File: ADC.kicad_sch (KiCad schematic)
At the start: 14 parts, among them J301 Conn_01x04_Pin, U301 ADS122C04IPW

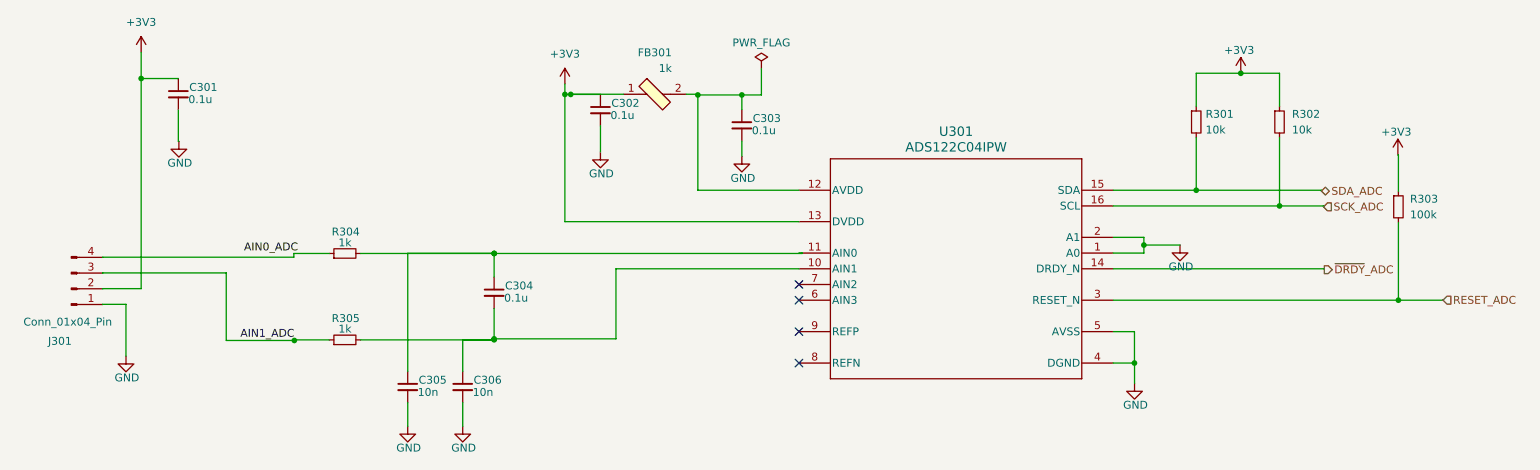
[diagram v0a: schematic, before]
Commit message: critical nets coloured,some tracks rerouted, section 9 completed.
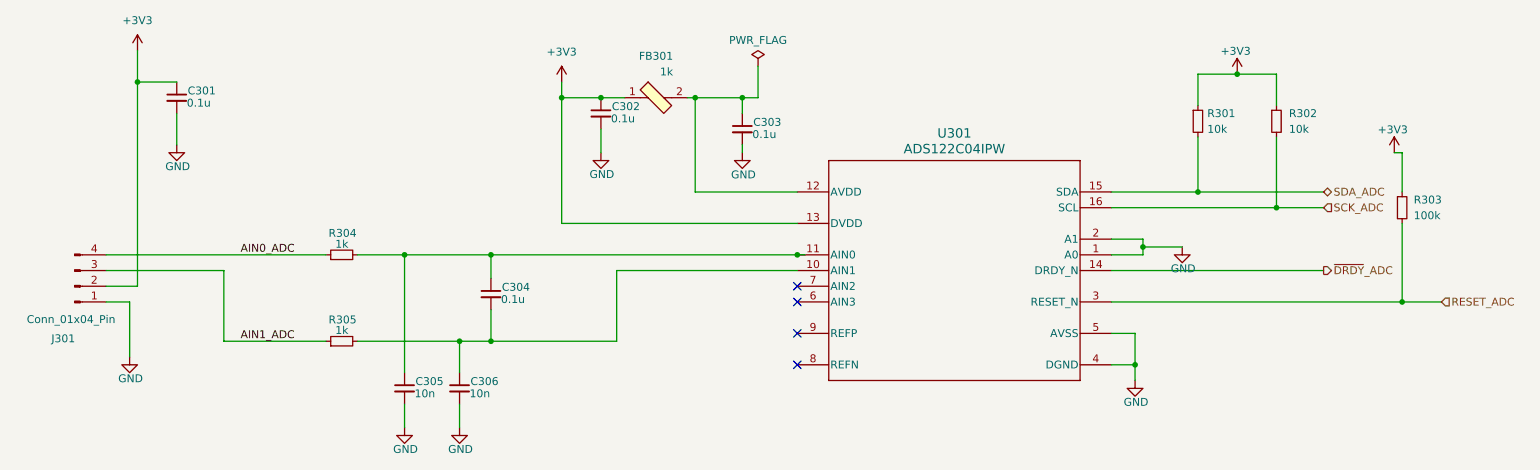
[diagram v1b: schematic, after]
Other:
- moved on the sheet: C301, C302, C303, C304, C305, C306, FB301, J301, R302, R303, R304, R305

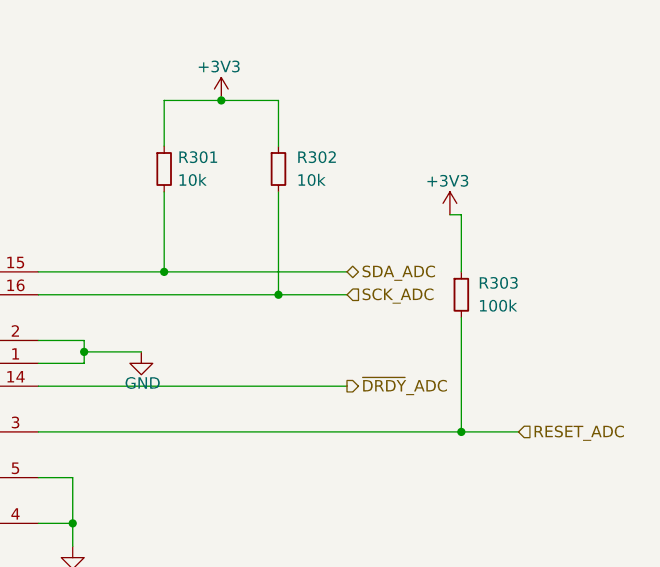
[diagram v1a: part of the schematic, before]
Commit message: I2C pins that is on ADC and DAC corrected
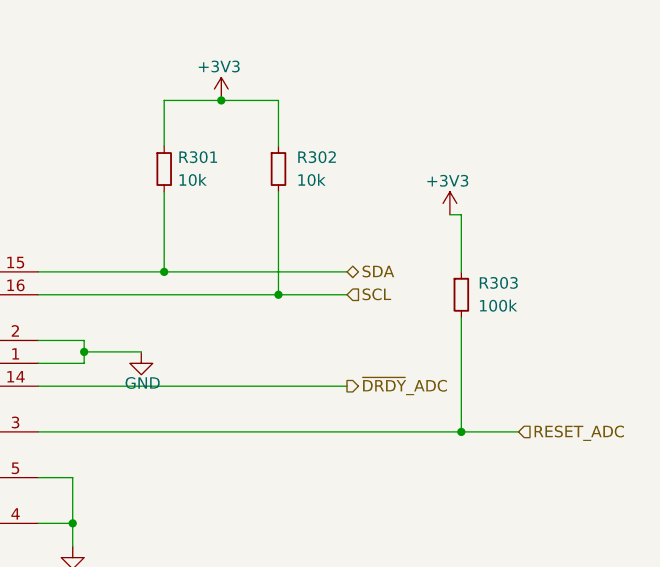
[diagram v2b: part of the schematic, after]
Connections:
- net SCK_ADC renamed SCL
- net SDA_ADC renamed SDA
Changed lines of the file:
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@@
 		)
 	)
-	(hierarchical_label "SCK_ADC"
+	(hierarchical_label "SCL"
 		(shape input)
 		(at 227.33 82.55 0)
@@
 		)
 	)
-	(hierarchical_label "SDA_ADC"
+	(hierarchical_label "SDA"
 		(shape bidirectional)
 		(at 227.33 80.01 0)

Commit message: schematic pages are reviewed
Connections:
- net AIN1: now reaches C304.2, C306.1, R305.2, U301.10 (AIN1)
- net AIN0: now reaches C304.1, C305.1, R304.2, U301.11 (AIN0)
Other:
- note added: "ADC"
- note added: "ADC CONN"
- moved on the sheet: C301, C302, C303, C304, C305, C306, FB301, J301, R301, R302, R303, R304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
